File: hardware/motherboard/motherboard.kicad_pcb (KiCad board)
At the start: 4 copper layers, 32.4 x 32 mm, 2 parts, among them U201 STM32MP157AACx, U401 K4E6E304ED-EGCG

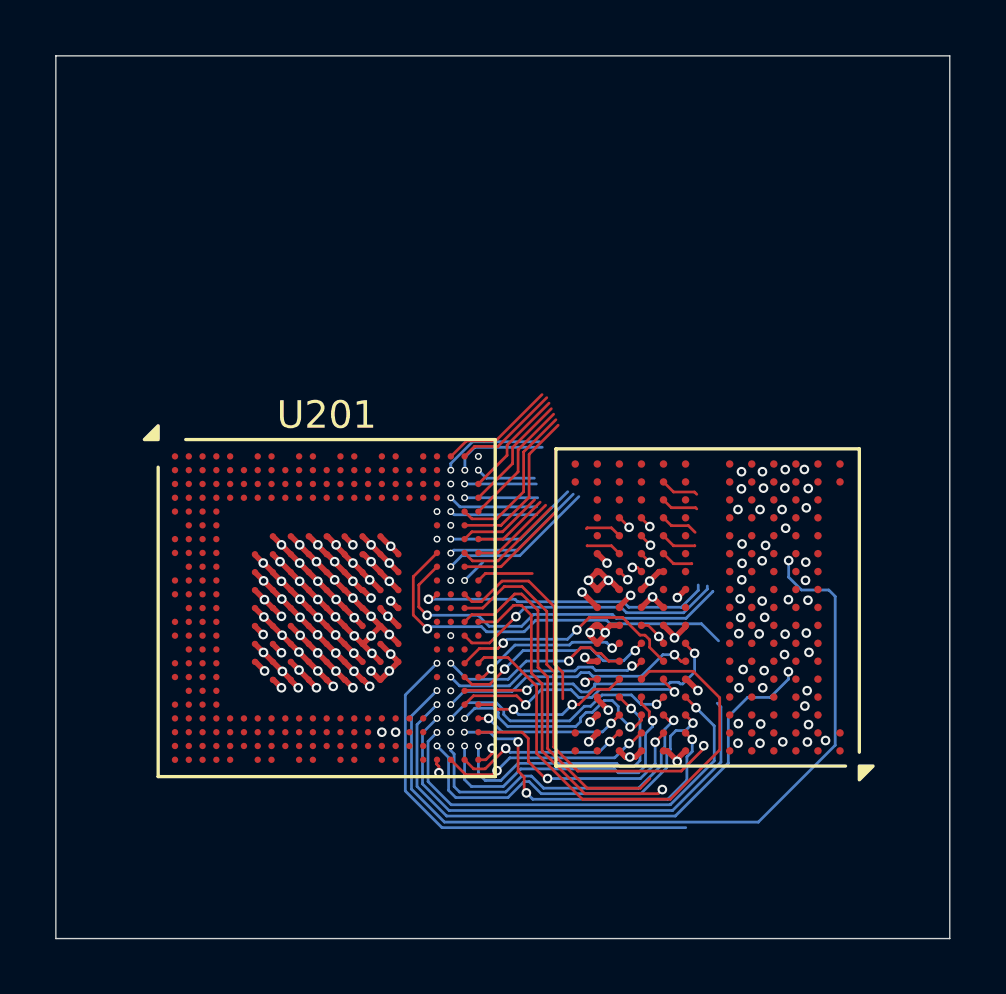
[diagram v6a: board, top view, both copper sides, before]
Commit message: route data lanes
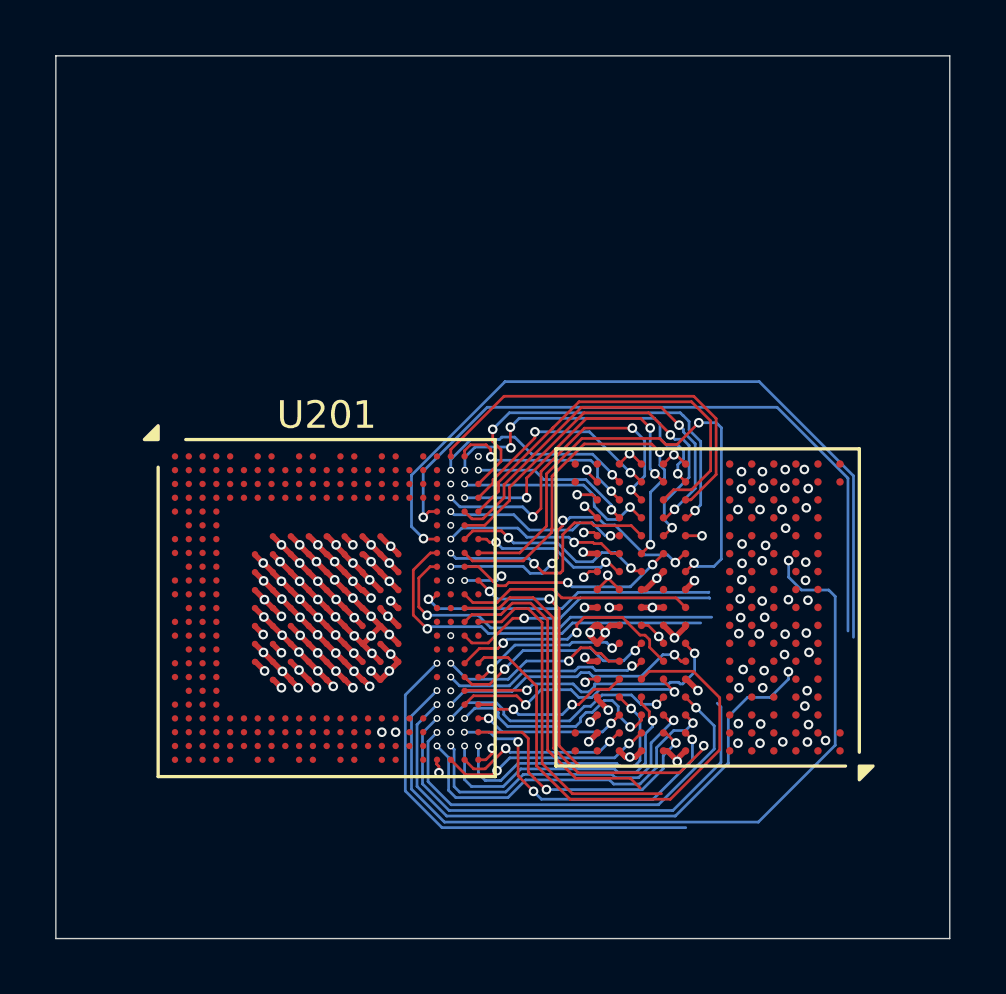
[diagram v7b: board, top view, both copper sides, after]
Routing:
- net /CPU/DDR.A9: track 0.00 -> 27.7 mm
- net /CPU/DDR.A7: track 0.00 -> 25.2 mm
- net /CPU/DDR.DQM0: track 3.16 -> 18.5 mm, vias 0 -> 2
- net /CPU/DDR.DQ20: track 4.24 -> 14.5 mm
- net /CPU/DDR.ZQ: track 2.06 -> 12.3 mm, vias 1 -> 3
- net /CPU/DDR.DQM2: track 3.99 -> 13.9 mm, vias 0 -> 2
- net /CPU/DDR.DQ6: track 4.50 -> 14.4 mm, vias 1 -> 2
- net /CPU/DDR.DQ22: track 3.25 -> 12.1 mm, vias 1 -> 4
- net /CPU/DDR.DQ21: track 6.00 -> 14.6 mm
- net /CPU/DDR.DQ16: track 3.43 -> 11.6 mm, vias 1 -> 4
- net /CPU/DDR.DQ1: track 7.10 -> 14.5 mm, vias 0 -> 2
- net /CPU/DDR.DQ0: track 7.12 -> 14.2 mm, vias 0 -> 2
- net /CPU/DDR.DQ17: track 4.04 -> 10.6 mm, vias 1 -> 4
- net /CPU/DDR.DQ4: track 5.70 -> 11.0 mm, vias 1 -> 4
- net /CPU/DDR.DQS2+: track 3.05 -> 7.52 mm
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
